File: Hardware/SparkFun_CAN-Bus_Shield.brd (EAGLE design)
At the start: 53.3 x 59.7 mm, 43 parts, among them Q1 16MHz, U1 USD-SOCKETNEW, U2 ARDUINO_R3_SHIELD, U3 JST_VERTICAL, U4 MCP2515, U5 MCP2551, U6 HEX_CONVERTER, X1 DB9 Plug

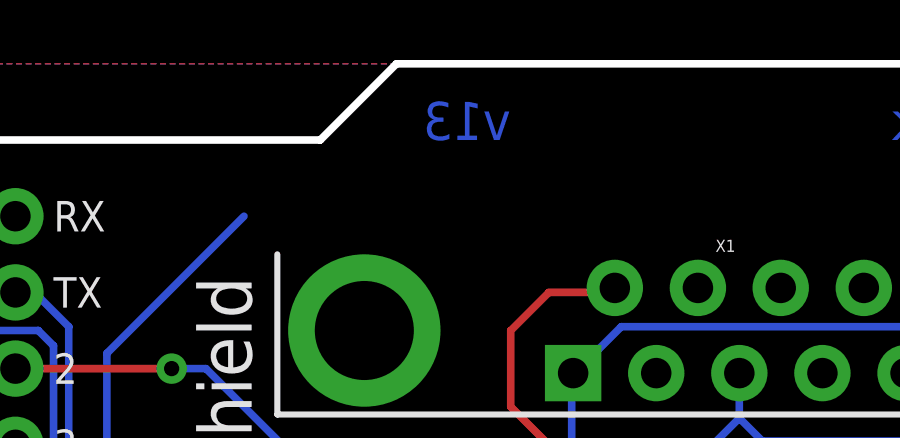
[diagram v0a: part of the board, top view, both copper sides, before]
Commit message: Schematic updates for QC checklist
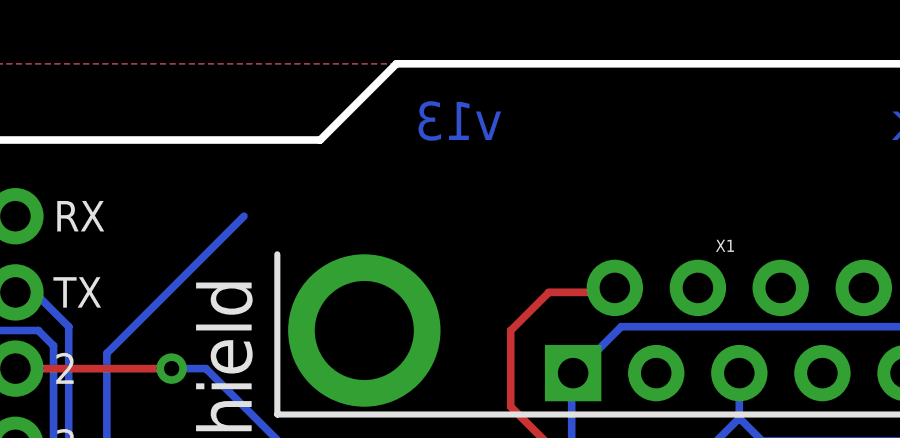
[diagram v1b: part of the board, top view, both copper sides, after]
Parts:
- FRAME1: value FRAME-LETTER -> (none)
- moved U$1 1.27 mm to (3.81, -26.7)
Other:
- board text removed: "Sukking Pang and Ryan Owens"
- board text removed: "v13"
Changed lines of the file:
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@@
 <layer number="251" name="SMDround" color="12" fill="11" visible="no" active="no"/>
 <layer number="254" name="cooling" color="7" fill="1" visible="no" active="yes"/>
+<layer number="255" name="routoute" color="7" fill="1" visible="no" active="yes"/>
 </layers>
 <board>
@@
 <text x="8.128" y="6.477" size="1.27" layer="21" font="vector" ratio="15">GPS</text>
 <text x="31.75" y="58.42" size="1.27" layer="16" font="vector" ratio="25" rot="MR180">www.skpang.co.uk</text>
-<text x="19.05" y="57.15" size="1.27" layer="16" font="vector" ratio="25" rot="MR0">v13</text>
 <text x="31.8135" y="33.782" size="1.27" layer="21" font="vector" ratio="15">PWR</text>
 <text x="25.654" y="33.782" size="1.27" layer="21" font="vector" ratio="15">D8</text>
 <text x="28.6385" y="33.782" size="1.27" layer="21" font="vector" ratio="15">D7</text>
-<text x="22.86" y="-24.13" size="1.778" layer="51" font="vector" ratio="15">Sukking Pang and Ryan Owens</text>
 <text x="45.72" y="19.685" size="1.27" layer="21" font="vector" ratio="15" rot="R180">U</text>
 <text x="44.577" y="7.493" size="1.27" layer="21" font="vector" ratio="15">D</text>
@@
 <text x="42.926" y="37.465" size="0.8128" layer="21" font="vector" ratio="15">L</text>
 <text x="5.334" y="7.62" size="1.016" layer="21" font="vector" ratio="15" rot="R180">GND</text>
-<text x="22.86" y="-27.94" size="1.778" layer="51" font="vector" ratio="15">Toni Klopfenstein</text>
+<text x="22.86" y="-26.67" size="1.778" layer="51" font="vector" ratio="15">Toni Klopfenstein</text>
 </plain>
 <attributes>
@@
 </element>
 <element name="JP5" library="SparkFun-Connectors" package="1X04" value="DNP" x="35.56" y="40.64"/>
-<element name="FRAME1" library="SparkFun-Aesthetics" package="CREATIVE_COMMONS" value="FRAME-LETTER" x="-7.89645625" y="-24.13"/>
-<element name="U$1" library="SparkFun-Aesthetics" package="REVISION" value="REVISION" x="3.81" y="-27.94"/>
+<element name="FRAME1" library="SparkFun-Aesthetics" package="CREATIVE_COMMONS" value="" x="-7.89645625" y="-24.13" smashed="yes">
+<attribute name="VERSION" value="v13" x="18.77354375" y="57.15" size="1.27" layer="16" font="vector" ratio="25" rot="SMR0"/>
+<attribute name="DESIGNER" value="Sukkin Pang and Ryan Owens" x="22.58354375" y="-24.13" size="1.778" layer="51"/>
+</element>
+<element name="U$1" library="SparkFun-Aesthetics" package="REVISION" value="REVISION" x="3.81" y="-26.67"/>
 <element name="LOGO1" library="SparkFun-Aesthetics" package="OSHW-LOGO-M" value="OSHW-LOGOM" x="40.64" y="44.45"/>
 <element name="SJ3" library="SparkFun-Passives" package="PAD-JUMPER-2-NC_BY_TRACE_YES_SILK" value="JUMPER-PAD-2-NC_BY_TRACE" x="3.81" y="5.08" rot="R90"/>

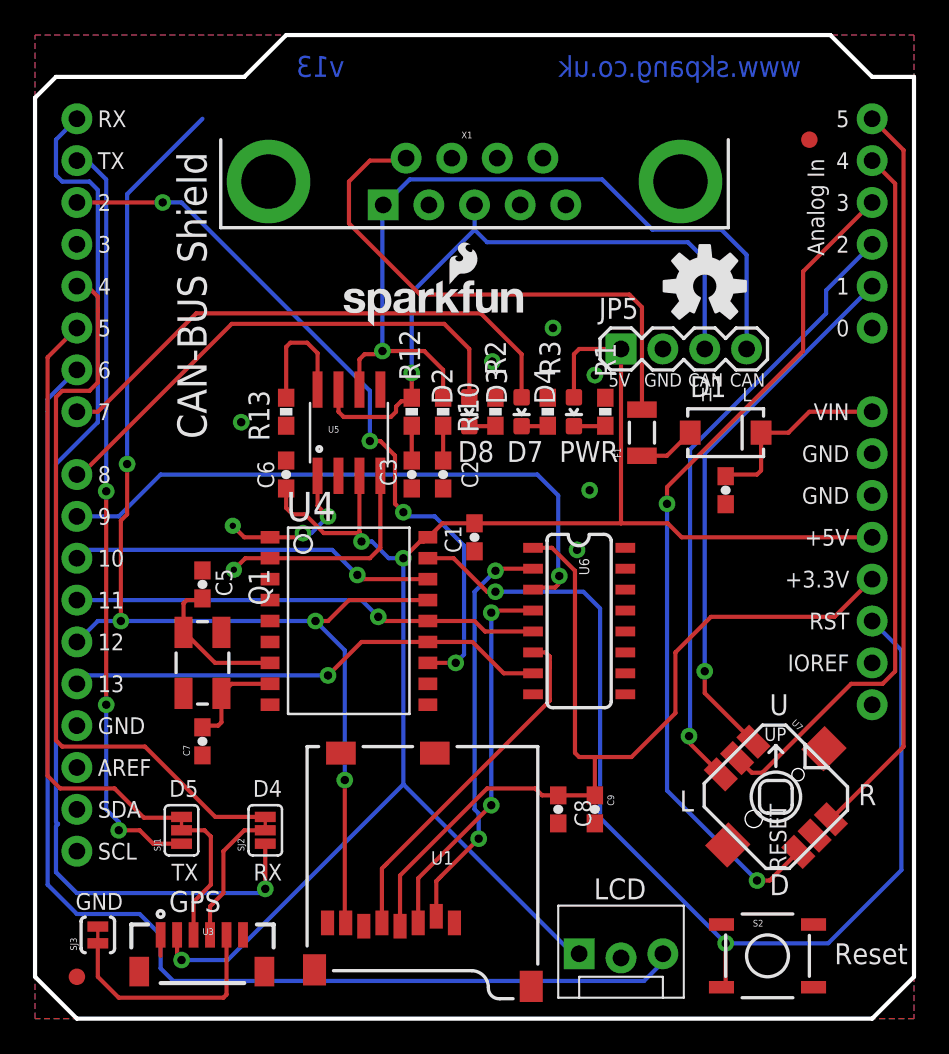
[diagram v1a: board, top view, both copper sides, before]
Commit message: Adding in OBDII/CAN jumpers
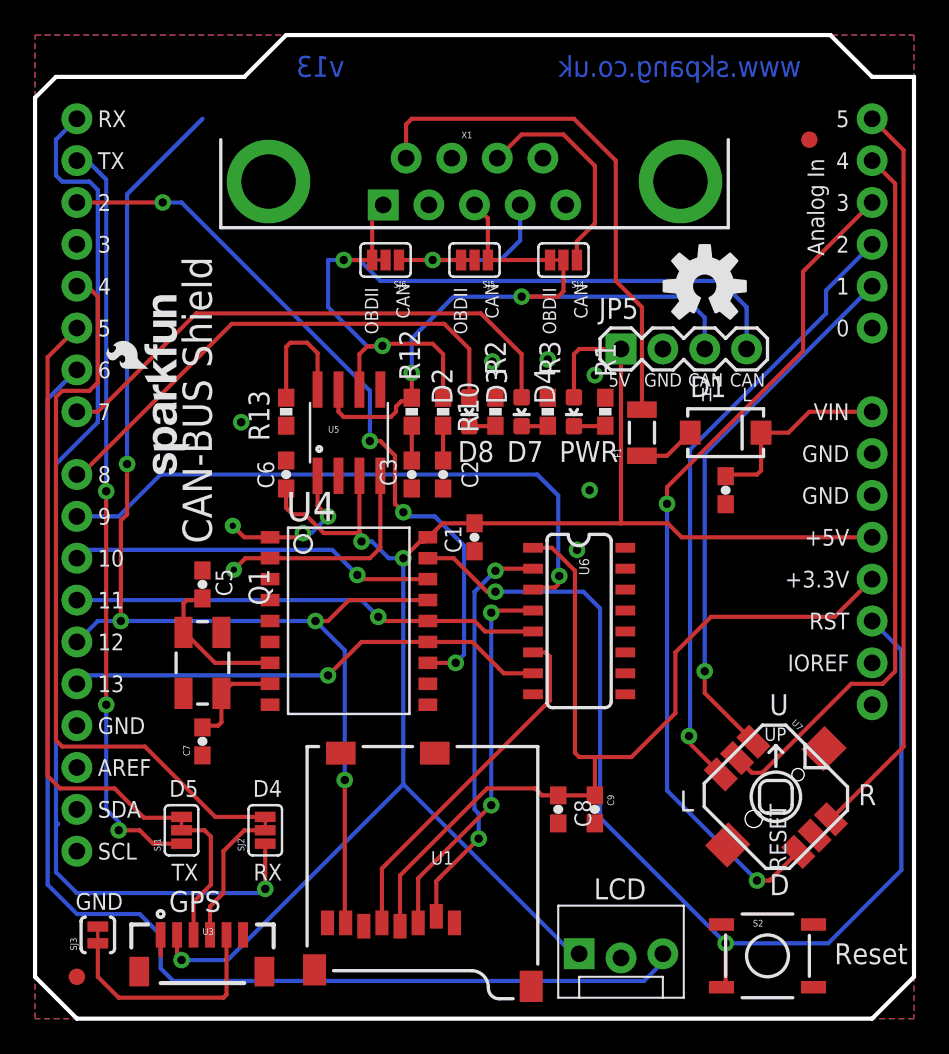
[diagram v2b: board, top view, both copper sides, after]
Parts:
- added FRAME2: (no value), SparkFun-Aesthetics:DUMMY
- added SJ4, SJ5, SJ6: JUMPER-PAD-3-2OF3_NC_BY_TRACE_SMALL, SparkFun-Passives:PAD-JUMPER-3-2OF3_NC_BY_TRACE_YES_SILK_FULL_BOX
- F1: value PTCTHERMISTOR1206 -> (none)
- moved JP4 12.8 mm to (9.53, 32.6), turned to 90 degrees
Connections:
- removed net NC4: X1.7
- new net N$2: SJ6.3, X1.5
- new net PIN2: SJ5.3, SJ6.1, X1.2
- new net PIN3: SJ4.3, SJ5.1, X1.3
- new net PIN7: SJ4.1, X1.7
- net CANH: now also SJ4.2; no longer X1.3
- net CANL: now also SJ6.2; no longer X1.5
- net GND: now also SJ5.2; no longer X1.2
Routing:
- net PIN7: track 0.00 -> 13.5 mm
- net PIN2: track 0.00 -> 11.7 mm, vias 0 -> 1
- net PIN3: track 0.00 -> 7.45 mm
- net CANH: track 40.2 -> 36.2 mm, vias 1 -> 2
- net N$2: track 0.00 -> 3.62 mm
- net N$13: track 32.7 -> 31.7 mm
- net CANL: track 48.5 -> 48.6 mm, vias 1 -> 2
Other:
- board text added: "OBDII"

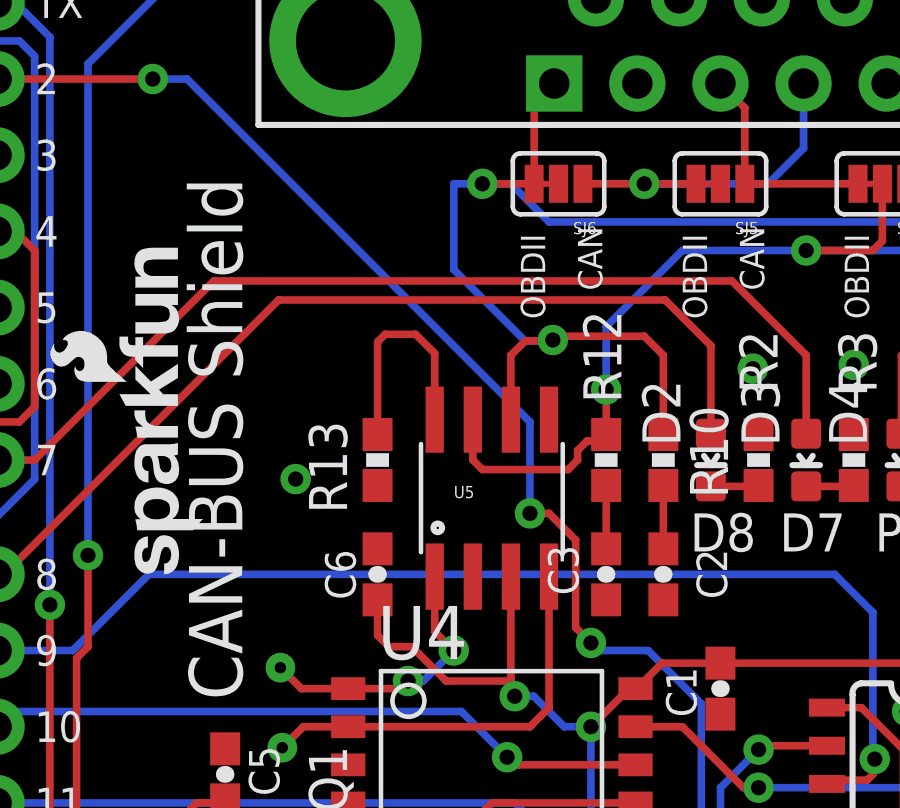
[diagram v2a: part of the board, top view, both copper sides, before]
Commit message: Adding ESD protection to CAN lines
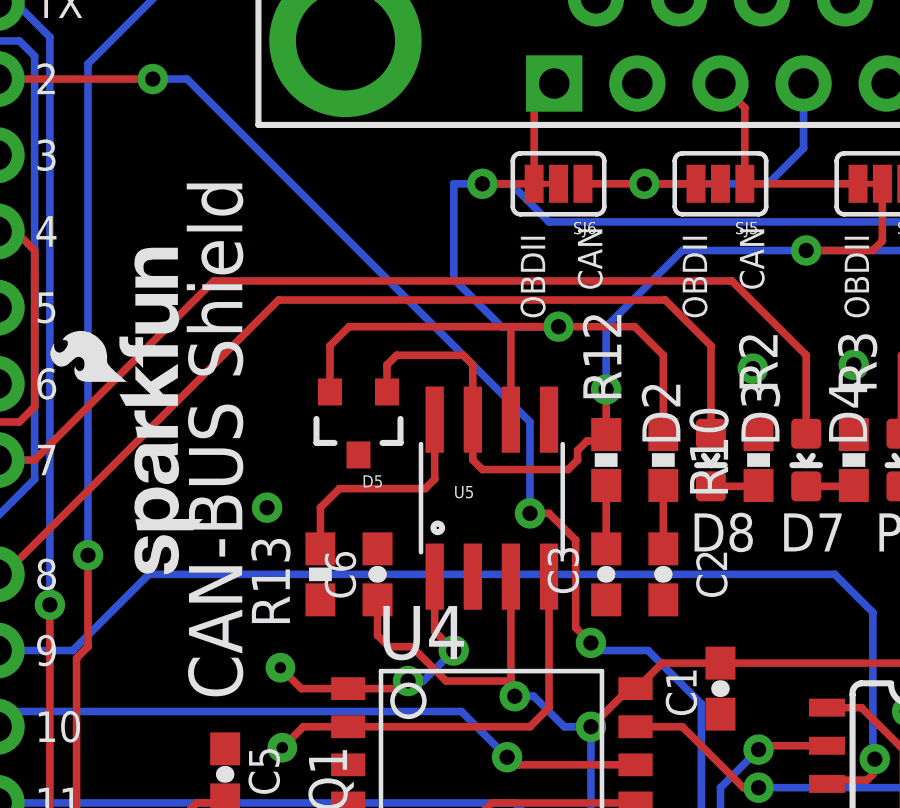
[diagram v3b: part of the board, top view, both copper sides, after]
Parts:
- added D5: PESD1CAN, Testing:SOT23-3
- moved R13 4.26 mm to (13.3, 33.0)
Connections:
- net CANH: now also D5.1
- net CANL: now also D5.2
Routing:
- net CANL: track 48.6 -> 57.4 mm
- net CANH: track 36.2 -> 42.0 mm
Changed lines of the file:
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@@
 <attribute name="PROD_ID" value="CAP-08749" x="22.86" y="33.02" size="1.778" layer="27" rot="R90" display="off"/>
 </element>
-<element name="R13" library="SparkFun-Resistors" package="0603-RES" value="4.7K" x="15.24" y="36.83" smashed="yes" rot="R90">
-<attribute name="NAME" x="14.224" y="35.052" size="1.27" layer="25" rot="R90"/>
-<attribute name="VALUE" value="4.7K" x="17.145" y="36.195" size="1.27" layer="27" rot="R90"/>
-<attribute name="PROD_ID" value="RES-07857" x="15.24" y="36.83" size="1.778" layer="27" rot="R90" display="off"/>
+<element name="R13" library="SparkFun-Resistors" package="0603-RES" value="4.7K" x="13.335" y="33.02" smashed="yes" rot="R90">
+<attribute name="NAME" x="12.319" y="31.242" size="1.27" layer="25" rot="R90"/>
+<attribute name="VALUE" value="4.7K" x="15.24" y="32.385" size="1.27" layer="27" rot="R90"/>
+<attribute name="PROD_ID" value="RES-07857" x="13.335" y="33.02" size="1.778" layer="27" rot="R90" display="off"/>
 </element>
 <element name="C6" library="SparkFun-Capacitors" package="0603-CAP" value="0.1uF" x="15.24" y="33.02" smashed="yes" rot="R270">
@@
 <element name="SJ5" library="SparkFun-Passives" package="PAD-JUMPER-3-2OF3_NC_BY_TRACE_YES_SILK_FULL_BOX" value="JUMPER-PAD-3-2OF3_NC_BY_TRACE_SMALL" x="26.67" y="46.0375" rot="R180"/>
 <element name="SJ6" library="SparkFun-Passives" package="PAD-JUMPER-3-2OF3_NC_BY_TRACE_YES_SILK_FULL_BOX" value="JUMPER-PAD-3-2OF3_NC_BY_TRACE_SMALL" x="21.2725" y="46.0375" rot="R180"/>
+<element name="D5" library="Testing" package="SOT23-3" value="PESD1CAN" x="14.605" y="38.1" rot="R180">
+<attribute name="PROD_ID" value="PROTO" x="14.605" y="38.1" size="1.778" layer="27" font="vector" ratio="15" rot="R180" display="off"/>
+</element>
 </elements>
 <signals>
@@
 <via x="32.893" y="28.448" extent="1-16" drill="0.508"/>
 <via x="27.7495" y="39.878" extent="1-16" drill="0.508"/>
-<via x="12.5095" y="36.195" extent="1-16" drill="0.508"/>
+<via x="11.557" y="35.2425" extent="1-16" drill="0.508"/>
 <polygon width="0.254" layer="16" isolate="0.3048">
 <vertex x="0" y="0"/>
@@
 <contactref element="U5" pad="8"/>
 <contactref element="R13" pad="2"/>
-<wire x1="16.51" y1="41.021" x2="15.494" y2="41.021" width="0.254" layer="1"/>
-<wire x1="15.494" y1="41.021" x2="15.24" y2="40.767" width="0.254" layer="1"/>
-<wire x1="15.24" y1="40.767" x2="15.24" y2="37.68" width="0.254" layer="1"/>
-<wire x1="17.145" y1="38.1762" x2="17.145" y2="40.386" width="0.254" layer="1"/>
-<wire x1="17.145" y1="40.386" x2="16.51" y2="41.021" width="0.254" layer="1"/>
+<wire x1="17.145" y1="38.1762" x2="17.145" y2="36.195" width="0.254" layer="1"/>
+<wire x1="17.145" y1="36.195" x2="16.8275" y2="35.8775" width="0.254" layer="1"/>
+<wire x1="16.8275" y1="35.8775" x2="13.97" y2="35.8775" width="0.254" layer="1"/>
+<wire x1="13.97" y1="35.8775" x2="13.335" y2="35.2425" width="0.254" layer="1"/>
+<wire x1="13.335" y1="35.2425" x2="13.335" y2="33.87" width="0.254" layer="1"/>
 </signal>
 <signal name="JOY-UP">
@@
 <wire x1="39.37" y1="43.815" x2="29.5275" y2="43.815" width="0.254" layer="16"/>
 <wire x1="25.4" y1="43.815" x2="29.5275" y2="43.815" width="0.254" layer="16"/>
+<contactref element="D5" pad="1"/>
+<wire x1="15.555" y1="39.1" x2="15.555" y2="40.0025" width="0.254" layer="1"/>
+<wire x1="15.555" y1="40.0025" x2="15.875" y2="40.3225" width="0.254" layer="1"/>
+<wire x1="15.875" y1="40.3225" x2="18.0975" y2="40.3225" width="0.254" layer="1"/>
+<wire x1="18.0975" y1="40.3225" x2="18.415" y2="40.005" width="0.254" layer="1"/>
+<wire x1="18.415" y1="40.005" x2="18.415" y2="38.1762" width="0.254" layer="1"/>
 </signal>
 <signal name="CANL">
@@
 <contactref element="R10" pad="2"/>
 <contactref element="JP5" pad="4"/>
-<via x="21.082" y="40.8305" extent="1-16" drill="0.508"/>
-<wire x1="19.685" y1="38.1762" x2="19.685" y2="40.3225" width="0.254" layer="1"/>
 <wire x1="24.765" y1="40.3225" x2="24.765" y2="37.68" width="0.254" layer="1"/>
 <contactref element="SJ6" pad="2"/>
-<wire x1="17.78" y1="46.0375" x2="17.78" y2="43.18" width="0.254" layer="16"/>
-<wire x1="24.765" y1="40.3225" x2="24.13" y2="40.9575" width="0.254" layer="1"/>
-<wire x1="24.13" y1="40.9575" x2="21.209" y2="40.9575" width="0.254" layer="1"/>
-<wire x1="21.209" y1="40.9575" x2="21.082" y2="40.8305" width="0.254" layer="1"/>
-<wire x1="19.685" y1="40.3225" x2="20.16125" y2="40.79875" width="0.254" layer="1"/>
-<wire x1="20.16125" y1="40.79875" x2="21.05025" y2="40.79875" width="0.254" layer="1"/>
-<wire x1="21.05025" y1="40.79875" x2="21.082" y2="40.8305" width="0.254" layer="1"/>
-<wire x1="17.78" y1="43.18" x2="20.16125" y2="40.79875" width="0.254" layer="16"/>
-<wire x1="20.16125" y1="40.79875" x2="21.05025" y2="40.79875" width="0.254" layer="16"/>
-<wire x1="21.05025" y1="40.79875" x2="21.082" y2="40.8305" width="0.254" layer="16"/>
+<wire x1="17.78" y1="46.0375" x2="17.78" y2="42.8625" width="0.254" layer="16"/>
 <wire x1="20.6375" y1="46.0375" x2="18.7325" y2="46.0375" width="0.254" layer="1"/>
 <via x="18.7325" y="46.0375" extent="1-16" drill="0.508"/>
@@
 <wire x1="41.5925" y1="44.7675" x2="43.18" y2="43.18" width="0.254" layer="16"/>
 <wire x1="43.18" y1="43.18" x2="43.18" y2="40.64" width="0.254" layer="16"/>
+<contactref element="D5" pad="2"/>
+<wire x1="13.655" y1="39.1" x2="13.655" y2="40.6425" width="0.254" layer="1"/>
+<wire x1="13.655" y1="40.6425" x2="14.2875" y2="41.275" width="0.254" layer="1"/>
+<wire x1="14.2875" y1="41.275" x2="19.3675" y2="41.275" width="0.254" layer="1"/>
+<wire x1="19.3675" y1="41.275" x2="19.685" y2="41.275" width="0.254" layer="1"/>
+<wire x1="19.685" y1="38.1762" x2="19.685" y2="41.275" width="0.254" layer="1"/>
+<wire x1="21.2725" y1="41.275" x2="23.8125" y2="41.275" width="0.254" layer="1"/>
+<wire x1="23.8125" y1="41.275" x2="24.765" y2="40.3225" width="0.254" layer="1"/>
+<wire x1="17.78" y1="42.8625" x2="19.3675" y2="41.275" width="0.254" layer="16"/>
+<wire x1="19.3675" y1="41.275" x2="21.2725" y2="41.275" width="0.254" layer="16"/>
+<via x="21.2725" y="41.275" extent="1-16" drill="0.508"/>
+<wire x1="21.2725" y1="41.275" x2="19.685" y2="41.275" width="0.254" layer="1"/>
 </signal>
 <signal name="A0">
